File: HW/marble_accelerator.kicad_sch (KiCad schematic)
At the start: 3 parts, among them J2 Conn_01x02_Pin, U2 CNY70, U5 L78L05_SO8

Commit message: initial commit of SW
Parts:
- added J3, J6: Conn_01x02_Pin, Connector_Phoenix_MC:PhoenixContact_MC_1,5_2-G-3.5_1x02_P3.50mm_Horizontal, symbol Connector:Conn_01x02_Pin
- added J4, J5: Conn_01x03_Pin, Connector_JST:JST_XH_B3B-XH-A_1x03_P2.50mm_Vertical, symbol Connector:Conn_01x03_Pin
- J2: footprint (none) -> Connector_Phoenix_MC:PhoenixContact_MC_1,5_2-G-3.5_1x02_P3.50mm_Horizontal
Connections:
- net coil driver/COIL0_NEG: now reaches J2.1 (Pin_1)
- net coil driver/COIL0_POS: now reaches J2.2 (Pin_2)
- new net coil driver/COIL1_NEG: J3.2 (Pin_2)
- new net coil driver/COIL1_POS: J3.1 (Pin_1)
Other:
- sheet coil driver ports: added COIL0_NEG, COIL0_POS, COIL1_NEG, COIL1_POS, IN_COIL0, IN_COIL1; removed none

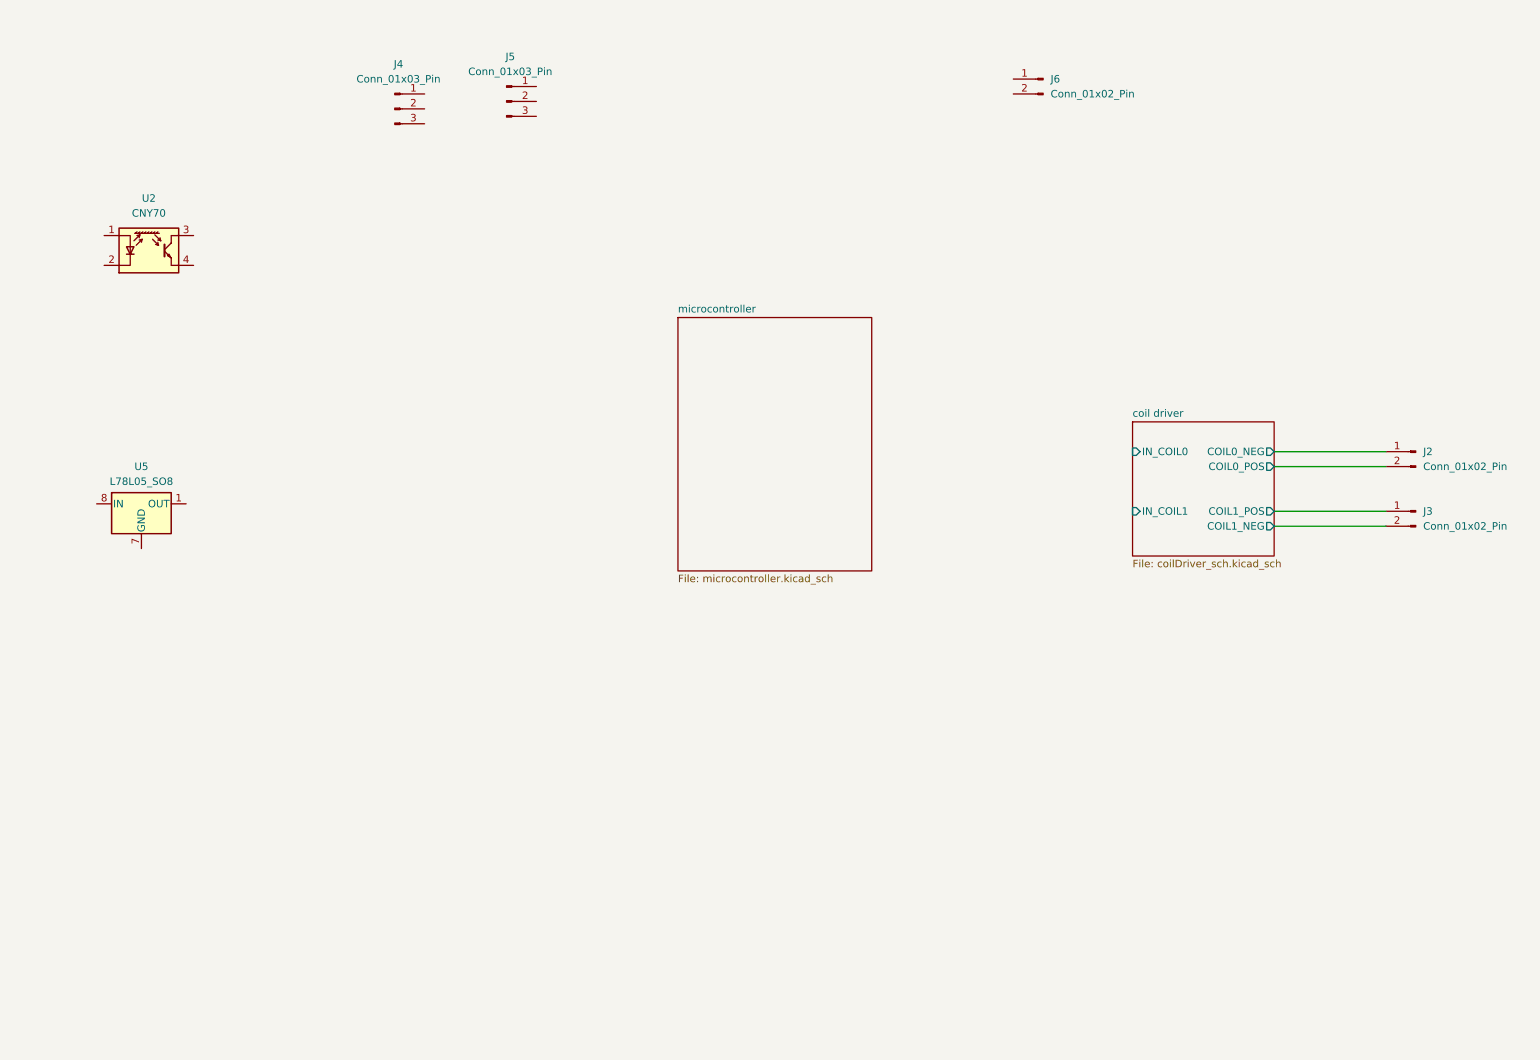
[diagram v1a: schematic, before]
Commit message: update schematic
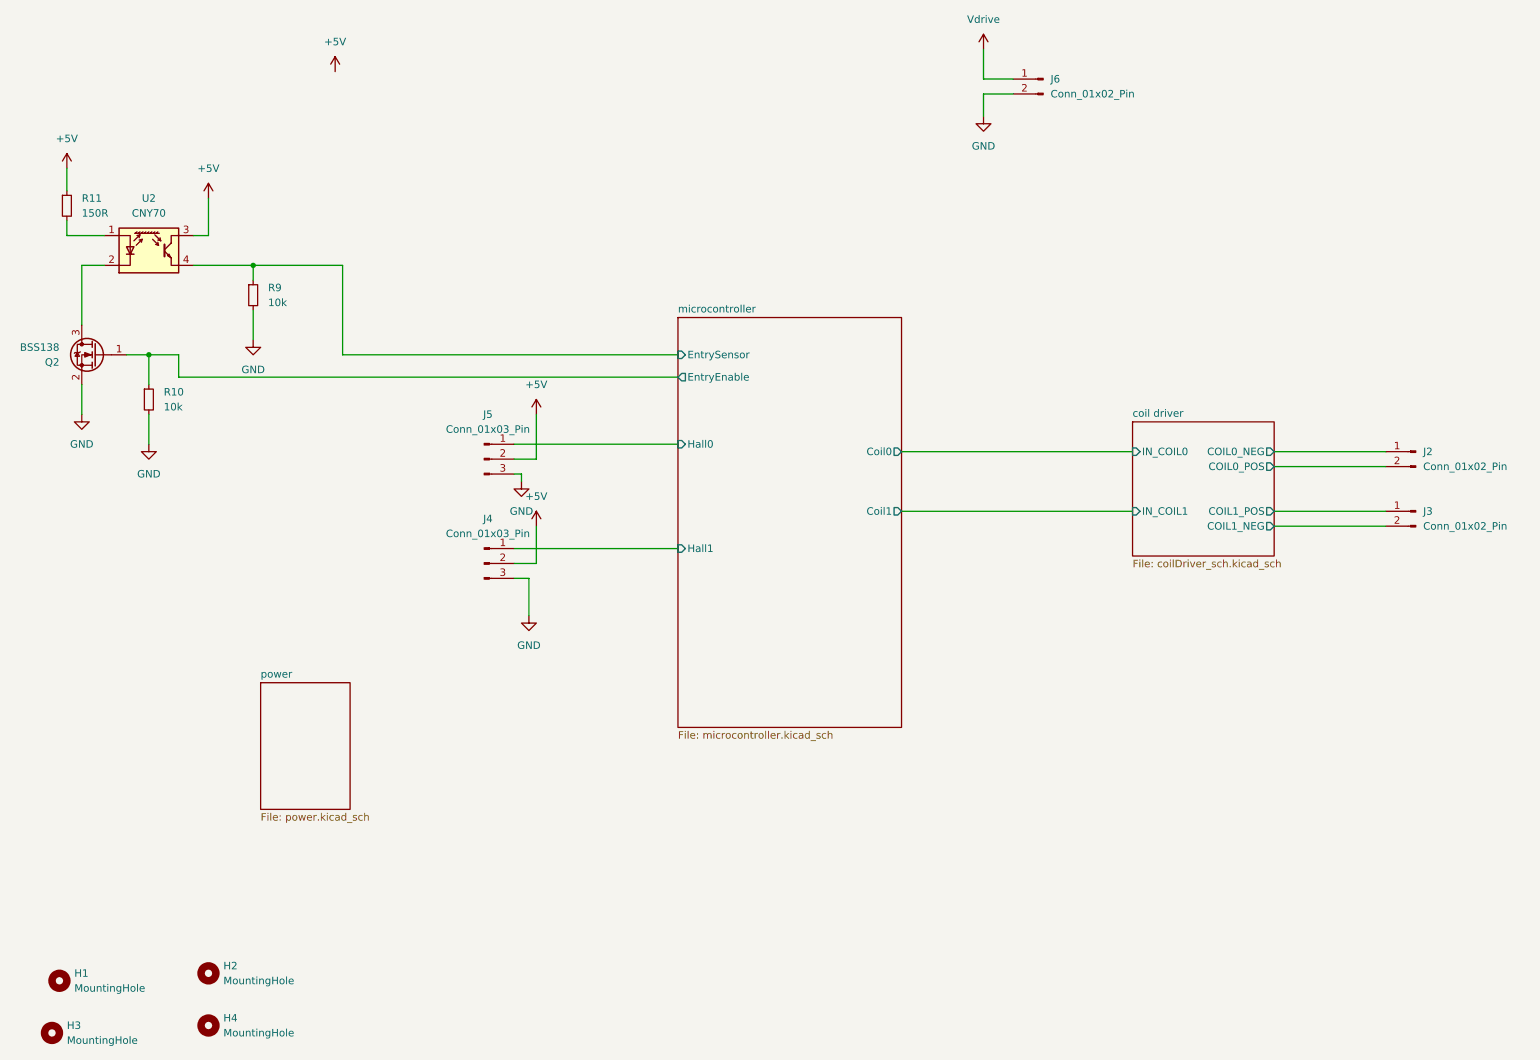
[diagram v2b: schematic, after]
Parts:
- removed U5: L78L05_SO8, Package_SO:SOIC-8_3.9x4.9mm_P1.27mm, symbol Regulator_Linear:L78L05_SO8
- added H1, H2, H3, H4: MountingHole, MountingHole:MountingHole_2.2mm_M2_DIN965, symbol Mechanical:MountingHole
- added Q2: BSS138, Package_TO_SOT_SMD:SOT-23, symbol Transistor_FET:BSS138
- added R10, R9: 10k, Capacitor_SMD:C_0603_1608Metric_Pad1.08x0.95mm_HandSolder, symbol Device:R_Small
- added R11: 150R, Capacitor_SMD:C_0603_1608Metric_Pad1.08x0.95mm_HandSolder, symbol Device:R_Small
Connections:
- net microcontroller/Hall1: now reaches J4.1 (Pin_1)
- net +5V: now reaches J4.2 (Pin_2)
- net +5V: now also J5.2 (Pin_2), U2.3 (C), R11.1
- net GND: now reaches J4.3 (Pin_3)
- net GND: now also J5.3 (Pin_3), J6.2 (Pin_2), Q2.2 (S), R10.2, R9.2
- net microcontroller/Hall0: now reaches J5.1 (Pin_1)
- net at U2.1 (A): now also R11.2
- net at U2.2 (K): now also Q2.3 (D)
- net microcontroller/EntrySensor: now reaches U2.4 (E)
- net microcontroller/EntrySensor: now also R9.1
- net Vdrive: now reaches J6.1 (Pin_1)
- new net microcontroller/EntryEnable: Q2.1 (G), R10.1
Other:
- added sheet power (power.kicad_sch)
- sheet microcontroller ports: added Coil0, Coil1, EntryEnable, EntrySensor, Hall0, Hall1; removed none
- moved on the sheet: J4, J5

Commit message: update HW, reduce board to 5x5 cm
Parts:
- H1, H2, H3, H4: footprint MountingHole:MountingHole_2.2mm_M2_DIN965 -> MountingHole:MountingHole_3.2mm_M3
- J2, J3, J6: footprint Connector_Phoenix_MC:PhoenixContact_MC_1,5_2-G-3.5_1x02_P3.50mm_Horizontal -> TerminalBlock_MetzConnect:TerminalBlock_MetzConnect_Type059_RT06302HBWC_1x02_P3.50mm_Horizontal
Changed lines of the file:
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@@
 			)
 		)
-		(property "Footprint" "MountingHole:MountingHole_2.2mm_M2_DIN965"
+		(property "Footprint" "MountingHole:MountingHole_3.2mm_M3"
 			(at 57.15 179.07 0)
 			(effects
@@
 			)
 		)
-		(property "Footprint" "MountingHole:MountingHole_2.2mm_M2_DIN965"
+		(property "Footprint" "MountingHole:MountingHole_3.2mm_M3"
 			(at 31.75 180.34 0)
 			(effects
@@
 			)
 		)
-		(property "Footprint" "Connector_Phoenix_MC:PhoenixContact_MC_1,5_2-G-3.5_1x02_P3.50mm_Horizontal"
+		(property "Footprint" "TerminalBlock_MetzConnect:TerminalBlock_MetzConnect_Type059_RT06302HBWC_1x02_P3.50mm_Horizontal"
 			(at 262.89 100.33 0)
 			(effects
@@
 			)
 		)
-		(property "Footprint" "MountingHole:MountingHole_2.2mm_M2_DIN965"
+		(property "Footprint" "MountingHole:MountingHole_3.2mm_M3"
 			(at 57.15 187.96 0)
 			(effects
@@
 			)
 		)
-		(property "Footprint" "Connector_Phoenix_MC:PhoenixContact_MC_1,5_2-G-3.5_1x02_P3.50mm_Horizontal"
+		(property "Footprint" "TerminalBlock_MetzConnect:TerminalBlock_MetzConnect_Type059_RT06302HBWC_1x02_P3.50mm_Horizontal"
 			(at 199.39 26.67 0)
 			(effects
@@
 			)
 		)
-		(property "Footprint" "Connector_Phoenix_MC:PhoenixContact_MC_1,5_2-G-3.5_1x02_P3.50mm_Horizontal"
+		(property "Footprint" "TerminalBlock_MetzConnect:TerminalBlock_MetzConnect_Type059_RT06302HBWC_1x02_P3.50mm_Horizontal"
 			(at 262.89 90.17 0)
 			(effects
@@
 			)
 		)
-		(property "Footprint" "MountingHole:MountingHole_2.2mm_M2_DIN965"
+		(property "Footprint" "MountingHole:MountingHole_3.2mm_M3"
 			(at 30.48 189.23 0)
 			(effects

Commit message: update layout and schematic
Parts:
- added R19, R20: 10k, Capacitor_SMD:C_0603_1608Metric_Pad1.08x0.95mm_HandSolder, symbol Device:R_Small
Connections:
- net microcontroller/Hall0: now also R19.2; no longer J5.1 (Pin_1)
- net microcontroller/Hall1: now also R20.2; no longer J4.1 (Pin_1)
- new net: J4.1 (Pin_1), R20.1
- new net: J5.1 (Pin_1), R19.1
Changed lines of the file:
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@@
 	(wire
 		(pts
-			(xy 109.22 106.68) (xy 137.16 106.68)
+			(xy 109.22 106.68) (xy 120.65 106.68)
 		)
 		(stroke
@@
 	(wire
 		(pts
+			(xy 125.73 88.9) (xy 137.16 88.9)
+		)
+		(stroke
+			(width 0)
+			(type default)
+		)
+	)
+	(wire
+		(pts
 			(xy 80.01 58.42) (xy 64.77 58.42)
 		)
@@
 	(wire
 		(pts
-			(xy 109.22 88.9) (xy 137.16 88.9)
+			(xy 109.22 88.9) (xy 120.65 88.9)
 		)
 		(stroke
@@
 		(pts
 			(xy 238.76 92.71) (xy 257.81 92.71)
+		)
+		(stroke
+			(width 0)
+			(type default)
+		)
+	)
+	(wire
+		(pts
+			(xy 125.73 106.68) (xy 137.16 106.68)
 		)
 		(stroke
@@
 				(path "/338fb3bb-e550-4c92-aa76-5d93a75fae71"
 					(reference "H2")
+					(unit 1)
+				)
+			)
+		)
+	)
+	(symbol
+		(lib_id "Device:R_Small")
+		(at 123.19 106.68 90)
+		(unit 1)
+		(exclude_from_sim no)
+		(in_bom yes)
+		(on_board yes)
+		(dnp no)
+		(fields_autoplaced yes)
+		(property "Reference" "R20"
+			(at 123.19 101.6 90)
+			(effects
+				(font
+					(size 1.27 1.27)
+				)
+			)
+		)
+		(property "Value" "10k"
+			(at 123.19 104.14 90)
+			(effects
+				(font
+					(size 1.27 1.27)
+				)
+			)
+		)
+		(property "Footprint" "Capacitor_SMD:C_0603_1608Metric_Pad1.08x0.95mm_HandSolder"
+			(at 123.19 106.68 0)
+			(effects
+				(font
+					(size 1.27 1.27)
+				)
+				(hide yes)
+			)
+		)
+		(property "Datasheet" "~"
+			(at 123.19 106.68 0)
+			(effects
+				(font
+					(size 1.27 1.27)
+				)
+				(hide yes)
+			)
+		)
+		(property "Description" "Resistor, small symbol"
+			(at 123.19 106.68 0)
+			(effects
+				(font
+					(size 1.27 1.27)
+				)
+				(hide yes)
+			)
+		)
+		(pin "2"
+		)
+		(pin "1"
+		)
+		(instances
+			(project "marble_accelerator"
+				(path "/338fb3bb-e550-4c92-aa76-5d93a75fae71"
+					(reference "R20")
 					(unit 1)
 				)
@@
 					(unit 1)
 				)
+			)
+		)
+	)
+	(symbol
+		(lib_id "Device:R_Small")
+		(at 123.19 88.9 90)
+		(unit 1)
+		(exclude_from_sim no)
+		(in_bom yes)
+		(on_board yes)
+		(dnp no)
+		(fields_autoplaced yes)
+		(property "Reference" "R19"
+			(at 123.19 83.82 90)
+			(effects
+				(font
+					(size 1.27 1.27)
+				)
+			)
+		)
+		(property "Value" "10k"
+			(at 123.19 86.36 90)
+			(effects
+				(font
+					(size 1.27 1.27)
+				)
+			)
+		)
+		(property "Footprint" "Capacitor_SMD:C_0603_1608Metric_Pad1.08x0.95mm_HandSolder"
+			(at 123.19 88.9 0)
+			(effects
+				(font
+					(size 1.27 1.27)
+				)
+				(hide yes)
+			)
+		)
+		(property "Datasheet" "~"
+			(at 123.19 88.9 0)
+			(effects
+				(font
+					(size 1.27 1.27)
+				)
+				(hide yes)
+			)
+		)
+		(property "Description" "Resistor, small symbol"
+			(at 123.19 88.9 0)
+			(effects
+				(font
+					(size 1.27 1.27)
+				)
+				(hide yes)
+			)
+		)
+		(pin "2"
+		)
+		(pin "1"
+		)
+		(instances
+			(project "marble_accelerator"
+				(path "/338fb3bb-e550-4c92-aa76-5d93a75fae71"
+					(reference "R19")
+					(unit 1)
+				)

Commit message: update schematic and board
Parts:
- renumbered H2 to H1, H1 to H2, H4 to H3, H3 to H4, J6 to J1, J5 to J3, J3 to J4, J4 to J5, Q2 to Q1, R11 to R1, R9 to R2, R10 to R3, R19 to R4, R20 to R5, U2 to U1
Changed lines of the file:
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@@
 		(dnp no)
 		(fields_autoplaced yes)
-		(property "Reference" "#PWR022"
+		(property "Reference" "#PWR010"
 			(at 110.49 101.6 0)
 			(effects
@@
 			(project "marble_accelerator"
 				(path "/338fb3bb-e550-4c92-aa76-5d93a75fae71"
-					(reference "#PWR022")
+					(reference "#PWR010")
 					(unit 1)
 				)
@@
 		(dnp no)
 		(fields_autoplaced yes)
-		(property "Reference" "#PWR016"
+		(property "Reference" "#PWR01"
 			(at 189.23 25.4 0)
 			(effects
@@
 			(project "marble_accelerator"
 				(path "/338fb3bb-e550-4c92-aa76-5d93a75fae71"
-					(reference "#PWR016")
+					(reference "#PWR01")
 					(unit 1)
 				)
@@
 		(dnp no)
 		(fields_autoplaced yes)
-		(property "Reference" "J4"
+		(property "Reference" "J5"
 			(at 104.775 101.6 0)
 			(effects
@@
 			(project ""
 				(path "/338fb3bb-e550-4c92-aa76-5d93a75fae71"
-					(reference "J4")
+					(reference "J5")
 					(unit 1)
 				)
@@
 		(dnp no)
 		(fields_autoplaced yes)
-		(property "Reference" "H2"
+		(property "Reference" "H1"
 			(at 59.69 177.7999 0)
 			(effects
@@
 			(project "marble_accelerator"
 				(path "/338fb3bb-e550-4c92-aa76-5d93a75fae71"
-					(reference "H2")
+					(reference "H1")
 					(unit 1)
 				)
@@
 		(dnp no)
 		(fields_autoplaced yes)
-		(property "Reference" "R20"
+		(property "Reference" "R5"
 			(at 123.19 101.6 90)
 			(effects
@@
 			(project "marble_accelerator"
 				(path "/338fb3bb-e550-4c92-aa76-5d93a75fae71"
-					(reference "R20")
+					(reference "R5")
 					(unit 1)
 				)
@@
 		(dnp no)
 		(fields_autoplaced yes)
-		(property "Reference" "J5"
+		(property "Reference" "J3"
 			(at 104.775 83.82 0)
 			(effects
@@
 			(project ""
 				(path "/338fb3bb-e550-4c92-aa76-5d93a75fae71"
-					(reference "J5")
-					(unit 1)
-				)
-			)
-		)
-	)
-	(symbol
-		(lib_id "power:+5V")
-		(at 78.74 25.4 0)
-		(unit 1)
-		(exclude_from_sim no)
-		(in_bom yes)
-		(on_board yes)
-		(dnp no)
-		(fields_autoplaced yes)
-		(property "Reference" "#PWR018"
-			(at 78.74 29.21 0)
-			(effects
-				(font
-					(size 1.27 1.27)
-				)
-				(hide yes)
-			)
-		)
-		(property "Value" "+5V"
-			(at 78.74 20.32 0)
-			(effects
-				(font
-					(size 1.27 1.27)
-				)
-			)
-		)
-		(property "Footprint" ""
-			(at 78.74 25.4 0)
-			(effects
-				(font
-					(size 1.27 1.27)
-				)
-				(hide yes)
-			)
-		)
-		(property "Datasheet" ""
-			(at 78.74 25.4 0)
-			(effects
-				(font
-					(size 1.27 1.27)
-				)
-				(hide yes)
-			)
-		)
-		(property "Description" "Power symbol creates a global label with name \"+5V\""
-			(at 78.74 25.4 0)
-			(effects
-				(font
-					(size 1.27 1.27)
-				)
-				(hide yes)
-			)
-		)
-		(pin "1"
-		)
-		(instances
-			(project ""
-				(path "/338fb3bb-e550-4c92-aa76-5d93a75fae71"
-					(reference "#PWR018")
+					(reference "J3")
 					(unit 1)
 				)
@@
 		(dnp no)
 		(fields_autoplaced yes)
-		(property "Reference" "H1"
+		(property "Reference" "H2"
 			(at 34.29 179.0699 0)
 			(effects
@@
 			(project ""
 				(path "/338fb3bb-e550-4c92-aa76-5d93a75fae71"
-					(reference "H1")
+					(reference "H2")
 					(unit 1)
 				)
@@
 		(dnp no)
 		(fields_autoplaced yes)
-		(property "Reference" "J3"
+		(property "Reference" "J4"
 			(at 264.16 100.3299 0)
 			(effects
@@
 			(project "marble_accelerator"
 				(path "/338fb3bb-e550-4c92-aa76-5d93a75fae71"
-					(reference "J3")
+					(reference "J4")
 					(unit 1)
 				)
@@
 		(dnp no)
 		(fields_autoplaced yes)
-		(property "Reference" "R9"
+		(property "Reference" "R2"
 			(at 67.31 62.2299 0)
 			(effects
@@
 			(project "marble_accelerator"
 				(path "/338fb3bb-e550-4c92-aa76-5d93a75fae71"
-					(reference "R9")
+					(reference "R2")
 					(unit 1)
 				)
@@
 		(dnp no)
 		(fields_autoplaced yes)
-		(property "Reference" "U2"
+		(property "Reference" "U1"
 			(at 46.99 46.99 0)
 			(effects
@@
 			(project ""
 				(path "/338fb3bb-e550-4c92-aa76-5d93a75fae71"
-					(reference "U2")
+					(reference "U1")
 					(unit 1)
 				)
@@
 		(dnp no)
 		(fields_autoplaced yes)
-		(property "Reference" "#PWR017"
+		(property "Reference" "#PWR03"
 			(at 189.23 39.37 0)
 			(effects
@@
 			(project ""
 				(path "/338fb3bb-e550-4c92-aa76-5d93a75fae71"
-					(reference "#PWR017")
+					(reference "#PWR03")
 					(unit 1)
 				)
@@
 		(dnp no)
 		(fields_autoplaced yes)
-		(property "Reference" "#PWR020"
+		(property "Reference" "#PWR011"
 			(at 113.03 106.68 0)
 			(effects
@@
 			(project "marble_accelerator"
 				(path "/338fb3bb-e550-4c92-aa76-5d93a75fae71"
-					(reference "#PWR020")
+					(reference "#PWR011")
 					(unit 1)
 				)
@@
 		(dnp no)
 		(fields_autoplaced yes)
-		(property "Reference" "H4"
+		(property "Reference" "H3"
 			(at 59.69 186.6899 0)
 			(effects
@@
 			(project "marble_accelerator"
 				(path "/338fb3bb-e550-4c92-aa76-5d93a75fae71"
-					(reference "H4")
+					(reference "H3")
 					(unit 1)
 				)
@@
 		(dnp no)
 		(fields_autoplaced yes)
-		(property "Reference" "R11"
+		(property "Reference" "R1"
 			(at 35.56 46.9899 0)
 			(effects
@@
 			(project "marble_accelerator"
 				(path "/338fb3bb-e550-4c92-aa76-5d93a75fae71"
-					(reference "R11")
+					(reference "R1")
 					(unit 1)
 				)
@@
 		(dnp no)
 		(fields_autoplaced yes)
-		(property "Reference" "#PWR034"
+		(property "Reference" "#PWR04"
 			(at 33.02 45.72 0)
 			(effects
@@
 			(project "marble_accelerator"
 				(path "/338fb3bb-e550-4c92-aa76-5d93a75fae71"
-					(reference "#PWR034")
+					(reference "#PWR04")
 					(unit 1)
 				)
@@
 		(dnp no)
 		(fields_autoplaced yes)
-		(property "Reference" "J6"
+		(property "Reference" "J1"
 			(at 200.66 26.6699 0)
 			(effects
@@
 			(project "marble_accelerator"
 				(path "/338fb3bb-e550-4c92-aa76-5d93a75fae71"
-					(reference "J6")
+					(reference "J1")
 					(unit 1)
 				)
@@
 		(dnp no)
 		(fields_autoplaced yes)
-		(property "Reference" "R19"
+		(property "Reference" "R4"
 			(at 123.19 83.82 90)
 			(effects
@@
 			(project "marble_accelerator"
 				(path "/338fb3bb-e550-4c92-aa76-5d93a75fae71"
-					(reference "R19")
+					(reference "R4")
 					(unit 1)
 				)
@@
 		(dnp no)
 		(fields_autoplaced yes)
-		(property "Reference" "#PWR036"
+		(property "Reference" "#PWR07"
 			(at 35.56 90.17 0)
 			(effects
@@
 			(project "marble_accelerator"
 				(path "/338fb3bb-e550-4c92-aa76-5d93a75fae71"
-					(reference "#PWR036")
+					(reference "#PWR07")
 					(unit 1)
 				)
@@
 		(dnp no)
 		(fields_autoplaced yes)
-		(property "Reference" "#PWR021"
+		(property "Reference" "#PWR012"
 			(at 111.76 124.46 0)
 			(effects
@@
 			(project "marble_accelerator"
 				(path "/338fb3bb-e550-4c92-aa76-5d93a75fae71"
-					(reference "#PWR021")
+					(reference "#PWR012")
 					(unit 1)
 				)
@@
 		(dnp no)
 		(fields_autoplaced yes)
-		(property "Reference" "H3"
+		(property "Reference" "H4"
 			(at 33.02 187.9599 0)
 			(effects
@@
 			(project "marble_accelerator"
 				(path "/338fb3bb-e550-4c92-aa76-5d93a75fae71"
-					(reference "H3")
+					(reference "H4")
 					(unit 1)
 				)
@@
 		(dnp no)
 		(fields_autoplaced yes)
-		(property "Reference" "#PWR038"
+		(property "Reference" "#PWR06"
 			(at 64.77 77.47 0)
 			(effects
@@
 			(project "marble_accelerator"
 				(path "/338fb3bb-e550-4c92-aa76-5d93a75fae71"
-					(reference "#PWR038")
+					(reference "#PWR06")
 					(unit 1)
 				)
@@
 		(dnp no)
 		(fields_autoplaced yes)
-		(property "Reference" "#PWR035"
+		(property "Reference" "#PWR05"
 			(at 57.15 50.8 0)
 			(effects
@@
 			(project "marble_accelerator"
 				(path "/338fb3bb-e550-4c92-aa76-5d93a75fae71"
-					(reference "#PWR035")
+					(reference "#PWR05")
 					(unit 1)
 				)
@@
 		(dnp no)
 		(fields_autoplaced yes)
-		(property "Reference" "R10"
+		(property "Reference" "R3"
 			(at 49.53 80.0099 0)
 			(effects
@@
 			(project "marble_accelerator"
 				(path "/338fb3bb-e550-4c92-aa76-5d93a75fae71"
-					(reference "R10")
+					(reference "R3")
 					(unit 1)
 				)
@@
 		(dnp no)
 		(fields_autoplaced yes)
-		(property "Reference" "#PWR037"
+		(property "Reference" "#PWR09"
 			(at 46.99 95.25 0)
 			(effects
@@
 			(project "marble_accelerator"
 				(path "/338fb3bb-e550-4c92-aa76-5d93a75fae71"
-					(reference "#PWR037")
+					(reference "#PWR09")
 					(unit 1)
 				)
@@
 		(on_board yes)
 		(dnp no)
-		(property "Reference" "Q2"
+		(property "Reference" "Q1"
 			(at 31.75 74.9301 0)
 			(effects
@@
 			(project ""
 				(path "/338fb3bb-e550-4c92-aa76-5d93a75fae71"
-					(reference "Q2")
+					(reference "Q1")
 					(unit 1)
 				)
@@
 		(dnp no)
 		(fields_autoplaced yes)
-		(property "Reference" "#PWR019"
+		(property "Reference" "#PWR08"
 			(at 113.03 87.63 0)
 			(effects
@@
 			(project "marble_accelerator"
 				(path "/338fb3bb-e550-4c92-aa76-5d93a75fae71"
-					(reference "#PWR019")
-					(unit 1)
-				)
+					(reference "#PWR08")
+					(unit 1)
+				)
